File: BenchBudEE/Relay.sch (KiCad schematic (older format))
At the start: 0 parts

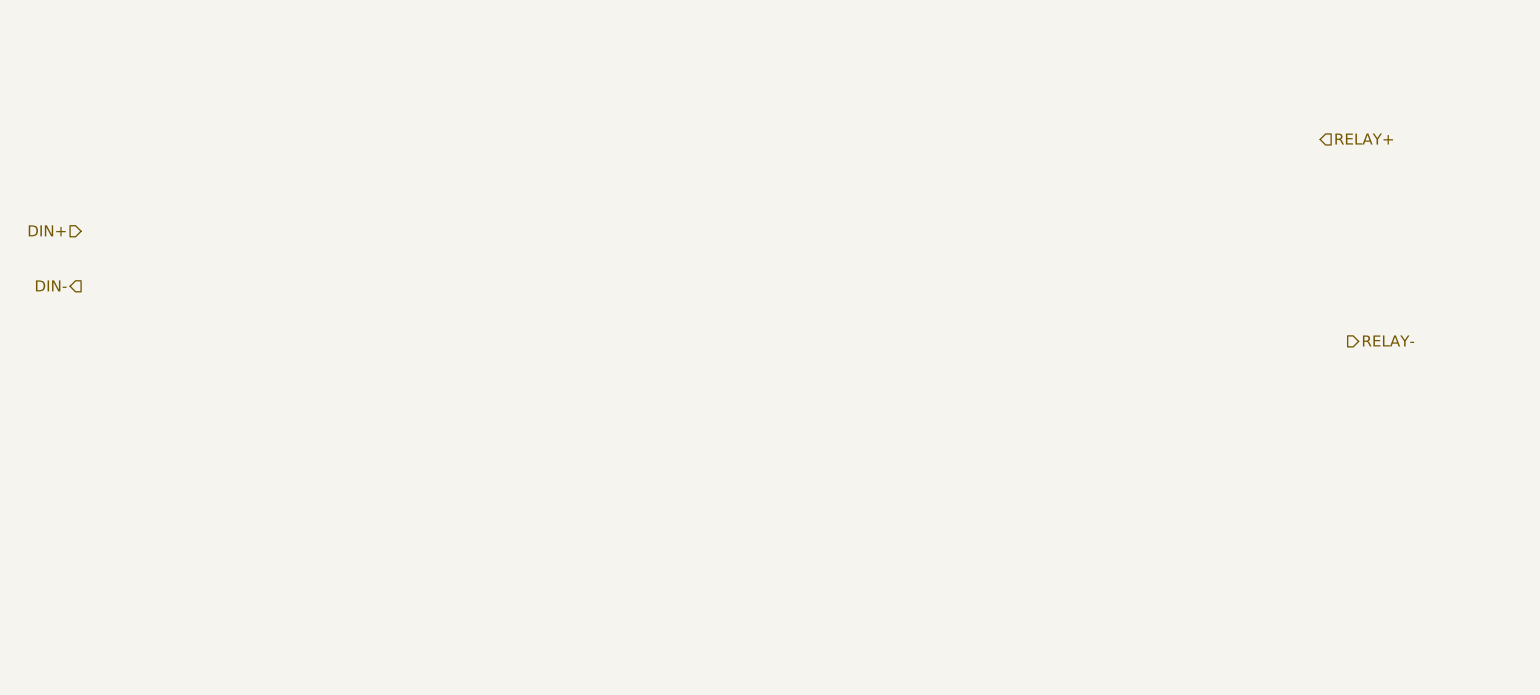
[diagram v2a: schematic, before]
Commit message: Created Relay block diagram
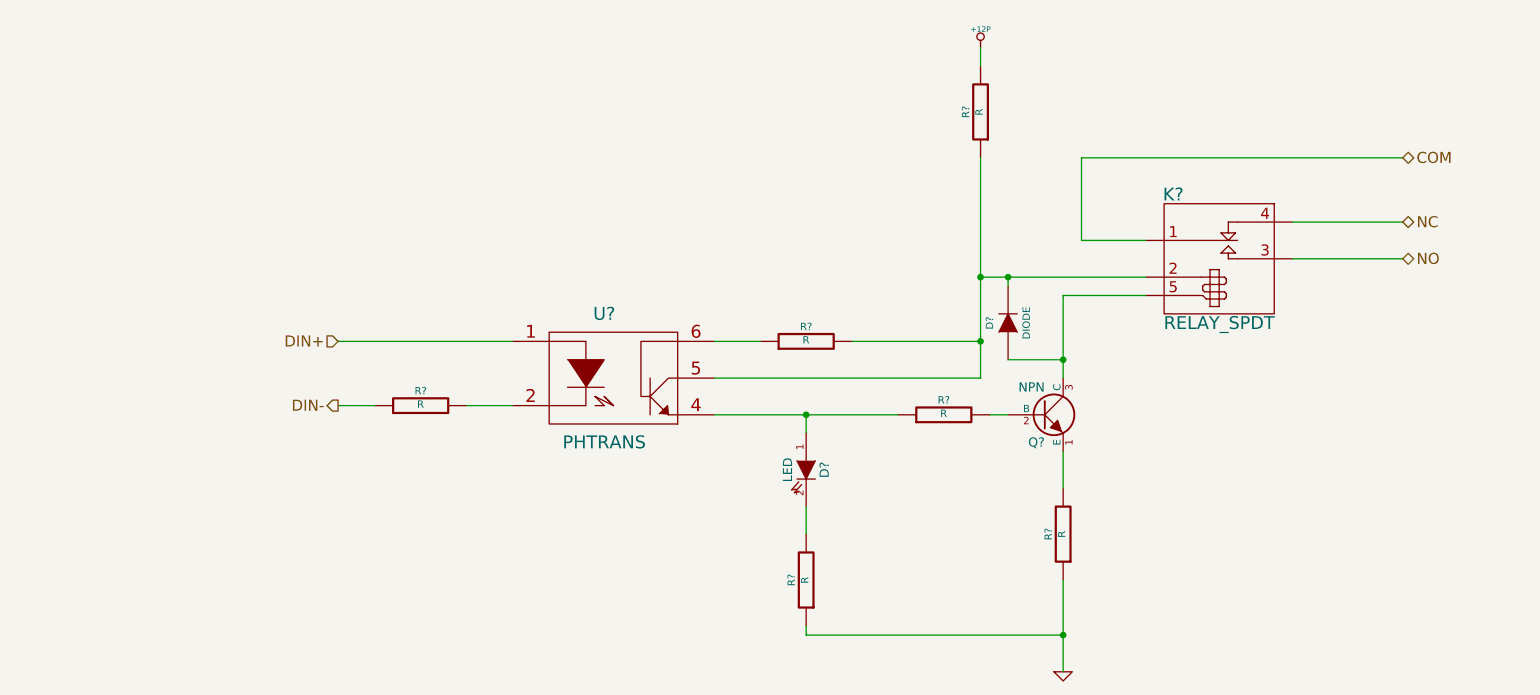
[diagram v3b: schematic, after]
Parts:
- added D?: LED, ~, symbol LED
- added D?: DIODE, ~, symbol DIODE
- added K?: RELAY_SPDT, ~, symbol RELAY_SPDT
- added Q?: NPN, ~, symbol NPN
- added R? (x6): R, ~, symbol R
- added U?: PHTRANS, ~, symbol PHTRANS
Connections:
- net DIN+: now also U?.1
- net DIN-: now also R?.1
- new net: D?.2 (K), K?.2 (COIL+), R?.1, R?.2, U?.5
- new net: D?.1 (A), K?.5 (COIL-), Q?.3 (C)
- new net: D?.1 (A), R?.1, U?.4
- new net: Q?.2 (B), R?.2
- new net: Q?.1 (E), R?.2
- new net: D?.2 (K), R?.2
- new net: R?.1, U?.6
- new net: R?.2, U?.2
- new net +12P: R?.2
- new net COM: K?.1 (COM)
- new net GND: R?.1, R?.1
- new net NC: K?.4 (NC)
- new net NO: K?.3 (NO)
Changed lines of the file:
@@
 LIBS:contrib
 LIBS:valves
+LIBS:CE Library
 LIBS:BenchBudEE-cache
 EELAYER 27 0
@@
 $Descr A4 11693 8268
 encoding utf-8
-Sheet 5 8
+Sheet 3 8
 Title ""
 Date "5 feb 2014"
@@
 Comment4 ""
 $EndDescr
-Text HLabel 2100 2950 0    60   Input ~ 0
+Text HLabel 3500 3550 0    60   Input ~ 0
 DIN+
-Text HLabel 2100 3250 0    60   Output ~ 0
+Text HLabel 3500 3900 0    60   Output ~ 0
 DIN-
-Text HLabel 9000 3550 2    60   Output ~ 0
-RELAY-
-Text HLabel 8850 2450 2    60   Input ~ 0
-RELAY+
+Text HLabel 9300 3100 2    60   BiDi ~ 0
+NO
+Text HLabel 9300 2900 2    60   BiDi ~ 0
+NC
+$Comp
+L PHTRANS U?
+U 1 1 52F2AEFF
+P 5000 3750
+F 0 "U?" H 4950 4100 70  0000 C CNN
+F 1 "PHTRANS" H 4950 3400 70  0000 C CNN
+F 2 "~" H 5000 3750 60  0000 C CNN
+F 3 "~" H 5000 3750 60  0000 C CNN
+	1    5000 3750
+	1    0    0    -1
+$EndComp
+$Comp
+L RELAY_SPDT K?
+U 1 1 52F29F66
+P 8300 3100
+F 0 "K?" H 8050 3450 70  0000 C CNN
+F 1 "RELAY_SPDT" H 8300 2750 70  0000 C CNN
+F 2 "~" H 8300 3250 60  0000 C CNN
+F 3 "~" H 8300 3250 60  0000 C CNN
+	1    8300 3100
+	1    0    0    -1
+$EndComp
+$Comp
+L R R?
+U 1 1 52F29F75
+P 6800 3950
+F 0 "R?" V 6880 3950 40  0000 C CNN
+F 1 "R" V 6807 3951 40  0000 C CNN
+F 2 "~" V 6730 3950 30  0000 C CNN
+F 3 "~" H 6800 3950 30  0000 C CNN
+	1    6800 3950
+	0    -1   -1   0
+$EndComp
+$Comp
+L NPN Q?
+U 1 1 52F29F84
+P 7350 3950
+F 0 "Q?" H 7350 3800 50  0000 R CNN
+F 1 "NPN" H 7350 4100 50  0000 R CNN
+F 2 "~" H 7350 3950 60  0000 C CNN
+F 3 "~" H 7350 3950 60  0000 C CNN
+	1    7350 3950
+	1    0    0    -1
+$EndComp
+$Comp
+L LED D?
+U 1 1 52F29F93
+P 6050 4250
+F 0 "D?" H 6050 4350 50  0000 C CNN
+F 1 "LED" H 6050 4150 50  0000 C CNN
+F 2 "~" H 6050 4250 60  0000 C CNN
+F 3 "~" H 6050 4250 60  0000 C CNN
+	1    6050 4250
+	0    1    1    0
+$EndComp
+Text HLabel 9300 2550 2    60   BiDi ~ 0
+COM
+$Comp
+L R R?
+U 1 1 52F2A010
+P 7450 4600
+F 0 "R?" V 7530 4600 40  0000 C CNN
+F 1 "R" V 7457 4601 40  0000 C CNN
+F 2 "~" V 7380 4600 30  0000 C CNN
+F 3 "~" H 7450 4600 30  0000 C CNN
+	1    7450 4600
+	-1   0    0    1
+$EndComp
+$Comp
+L GND #PWR?
+U 1 1 52F2A023
+P 7450 5350
+F 0 "#PWR?" H 7450 5350 30  0001 C CNN
+F 1 "GND" H 7450 5280 30  0001 C CNN
+F 2 "" H 7450 5350 60  0000 C CNN
+F 3 "" H 7450 5350 60  0000 C CNN
+	1    7450 5350
+	1    0    0    -1
+$EndComp
+$Comp
+L R R?
+U 1 1 52F2A068
+P 6050 4850
+F 0 "R?" V 6130 4850 40  0000 C CNN
+F 1 "R" V 6057 4851 40  0000 C CNN
+F 2 "~" V 5980 4850 30  0000 C CNN
+F 3 "~" H 6050 4850 30  0000 C CNN
+	1    6050 4850
+	-1   0    0    1
+$EndComp
+$Comp
+L R R?
+U 1 1 52F2A0AD
+P 6050 3550
+F 0 "R?" V 6130 3550 40  0000 C CNN
+F 1 "R" V 6057 3551 40  0000 C CNN
+F 2 "~" V 5980 3550 30  0000 C CNN
+F 3 "~" H 6050 3550 30  0000 C CNN
+	1    6050 3550
+	0    -1   -1   0
+$EndComp
+$Comp
+L R R?
+U 1 1 52F2A0C7
+P 7000 2300
+F 0 "R?" V 7080 2300 40  0000 C CNN
+F 1 "R" V 7007 2301 40  0000 C CNN
+F 2 "~" V 6930 2300 30  0000 C CNN
+F 3 "~" H 7000 2300 30  0000 C CNN
+	1    7000 2300
+	-1   0    0    1
+$EndComp
+$Comp
+L R R?
+U 1 1 52F2A0F9
+P 3950 3900
+F 0 "R?" V 4030 3900 40  0000 C CNN
+F 1 "R" V 3957 3901 40  0000 C CNN
+F 2 "~" V 3880 3900 30  0000 C CNN
+F 3 "~" H 3950 3900 30  0000 C CNN
+	1    3950 3900
+	0    -1   -1   0
+$EndComp
+$Comp
+L +12P #PWR?
+U 1 1 52F2A164
+P 7000 1950
+F 0 "#PWR?" H 7000 1920 30  0001 C CNN
+F 1 "+12P" H 7000 2050 30  0000 C CNN
+F 2 "" H 7000 1950 60  0000 C CNN
+F 3 "" H 7000 1950 60  0000 C CNN
+	1    7000 1950
+	1    0    0    -1
+$EndComp
+$Comp
+L DIODE D?
+U 1 1 52F2A1DE
+P 7150 3450
+F 0 "D?" H 7150 3550 40  0000 C CNN
+F 1 "DIODE" H 7150 3350 40  0000 C CNN
+F 2 "~" H 7150 3450 60  0000 C CNN
+F 3 "~" H 7150 3450 60  0000 C CNN
+	1    7150 3450
+	0    -1   -1   0
+$EndComp
+Wire Wire Line
+	8700 3100 9300 3100
+Wire Wire Line
+	8700 2900 9300 2900
+Wire Wire Line
+	6050 3950 6550 3950
+Wire Wire Line
+	7050 3950 7150 3950
+Wire Wire Line
+	7450 4150 7450 4350
+Wire Wire Line
+	7450 3750 7450 3650
+Wire Wire Line
+	7450 3650 7450 3300
+Wire Wire Line
+	7450 3300 7900 3300
+Wire Wire Line
+	7900 3200 7150 3200
+Wire Wire Line
+	7150 3200 7000 3200
+Wire Wire Line
+	7000 2550 7000 3200
+Wire Wire Line
+	7000 3200 7000 3550
+Wire Wire Line
+	7000 3550 7000 3750
+Wire Wire Line
+	7450 4850 7450 5150
+Wire Wire Line
+	7450 5150 7450 5350
+Wire Wire Line
+	6050 4450 6050 4600
+Wire Wire Line
+	6050 5100 6050 5150
+Wire Wire Line
+	6050 5150 7450 5150
+Connection ~ 7450 5150
+Wire Wire Line
+	7000 3750 5550 3750
+Connection ~ 7000 3200
+Wire Wire Line
+	5550 3550 5800 3550
+Wire Wire Line
+	6300 3550 7000 3550
+Connection ~ 7000 3550
+Wire Wire Line
+	4200 3900 4450 3900
+Wire Wire Line
+	3700 3900 3500 3900
+Wire Wire Line
+	3500 3550 4450 3550
+Wire Wire Line
+	7000 1950 7000 2050
+Wire Wire Line
+	9300 2550 7550 2550
+Wire Wire Line
+	7550 2550 7550 3000
+Wire Wire Line
+	7550 3000 7900 3000
+Wire Wire Line
+	7150 3650 7450 3650
+Connection ~ 7450 3650
+Wire Wire Line
+	7150 3250 7150 3200
+Connection ~ 7150 3200
+Wire Wire Line
+	5550 3950 6050 3950
+Wire Wire Line
+	6050 4050 6050 3950
+Connection ~ 6050 3950
 $EndSCHEMATC

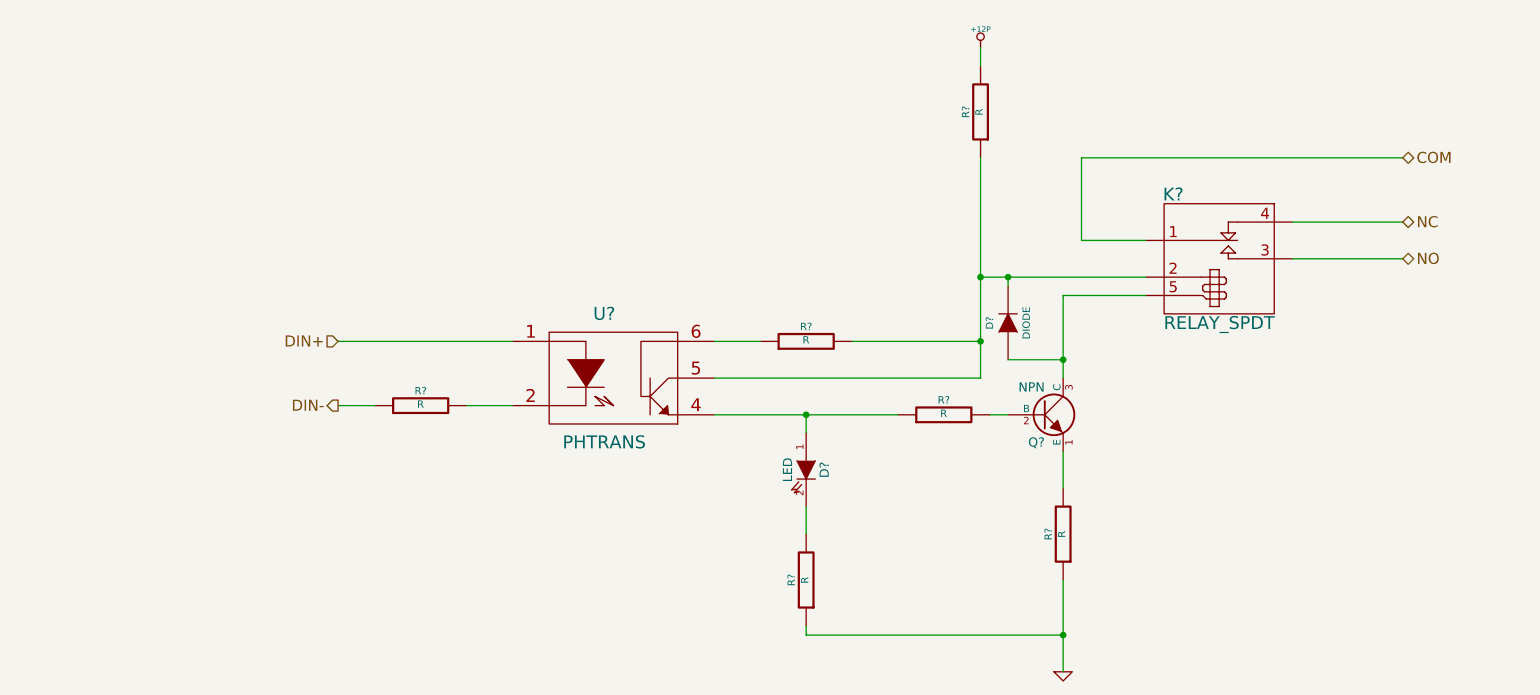
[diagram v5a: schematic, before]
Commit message: Schematic modules connected together and to arduino pins
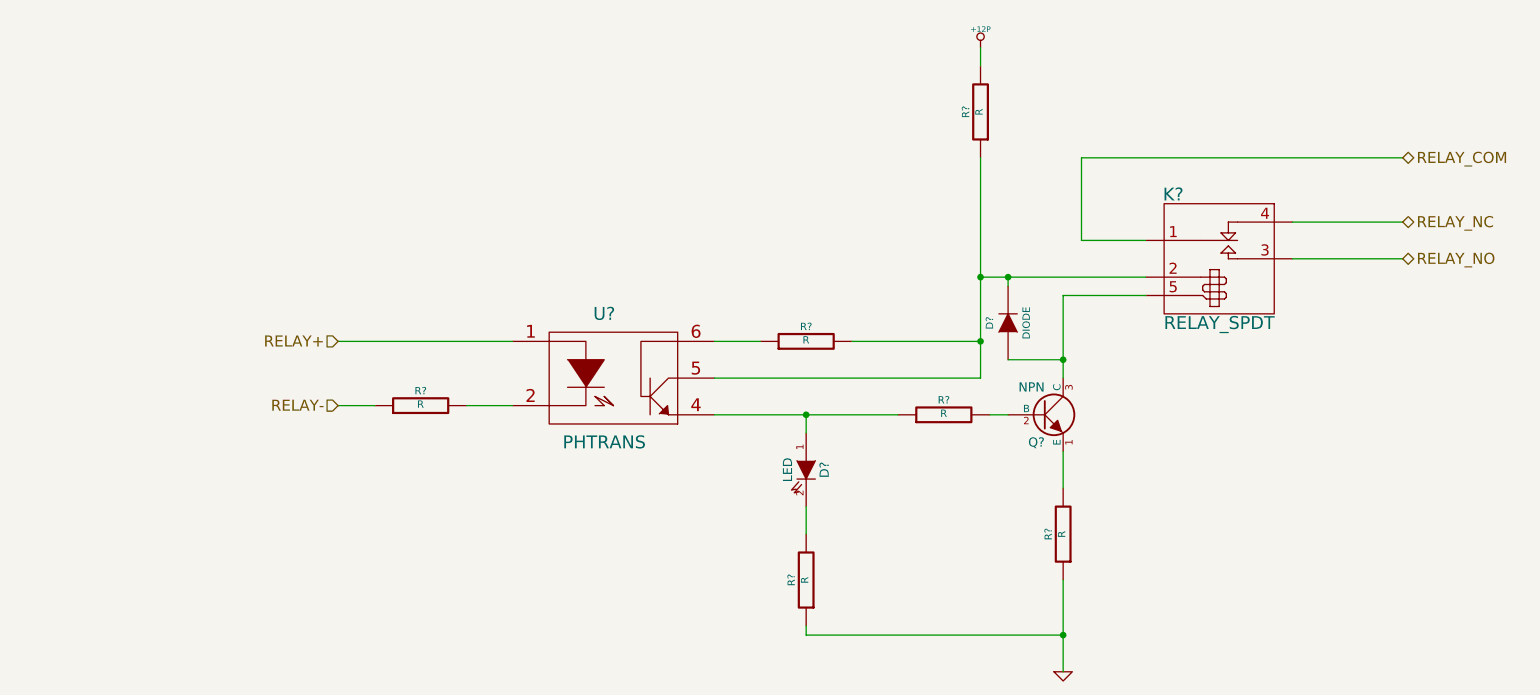
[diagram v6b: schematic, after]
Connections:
- net COM renamed RELAY_COM
- net DIN+ renamed RELAY+
- net DIN- renamed RELAY-
- net NC renamed RELAY_NC
- net NO renamed RELAY_NO
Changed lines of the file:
@@
 LIBS:valves
 LIBS:CE Library
+LIBS:atx_24pin_power
 LIBS:BenchBudEE-cache
 EELAYER 27 0
@@
 $Descr A4 11693 8268
 encoding utf-8
-Sheet 3 9
+Sheet 2 9
 Title ""
-Date "6 feb 2014"
+Date "8 feb 2014"
 Rev ""
 Comp ""
@@
 $EndDescr
 Text HLabel 3500 3550 0    60   Input ~ 0
-DIN+
-Text HLabel 3500 3900 0    60   Output ~ 0
-DIN-
+RELAY+
+Text HLabel 3500 3900 0    60   Input ~ 0
+RELAY-
 Text HLabel 9300 3100 2    60   BiDi ~ 0
-NO
+RELAY_NO
 Text HLabel 9300 2900 2    60   BiDi ~ 0
-NC
+RELAY_NC
 $Comp
 L PHTRANS U?
@@
 $EndComp
 Text HLabel 9300 2550 2    60   BiDi ~ 0
-COM
+RELAY_COM
 $Comp
 L R R?
